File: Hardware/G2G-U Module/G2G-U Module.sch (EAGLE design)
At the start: 4 parts, among them J1 GROVE-4P-2.0-SMD-FEMALE-REINF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

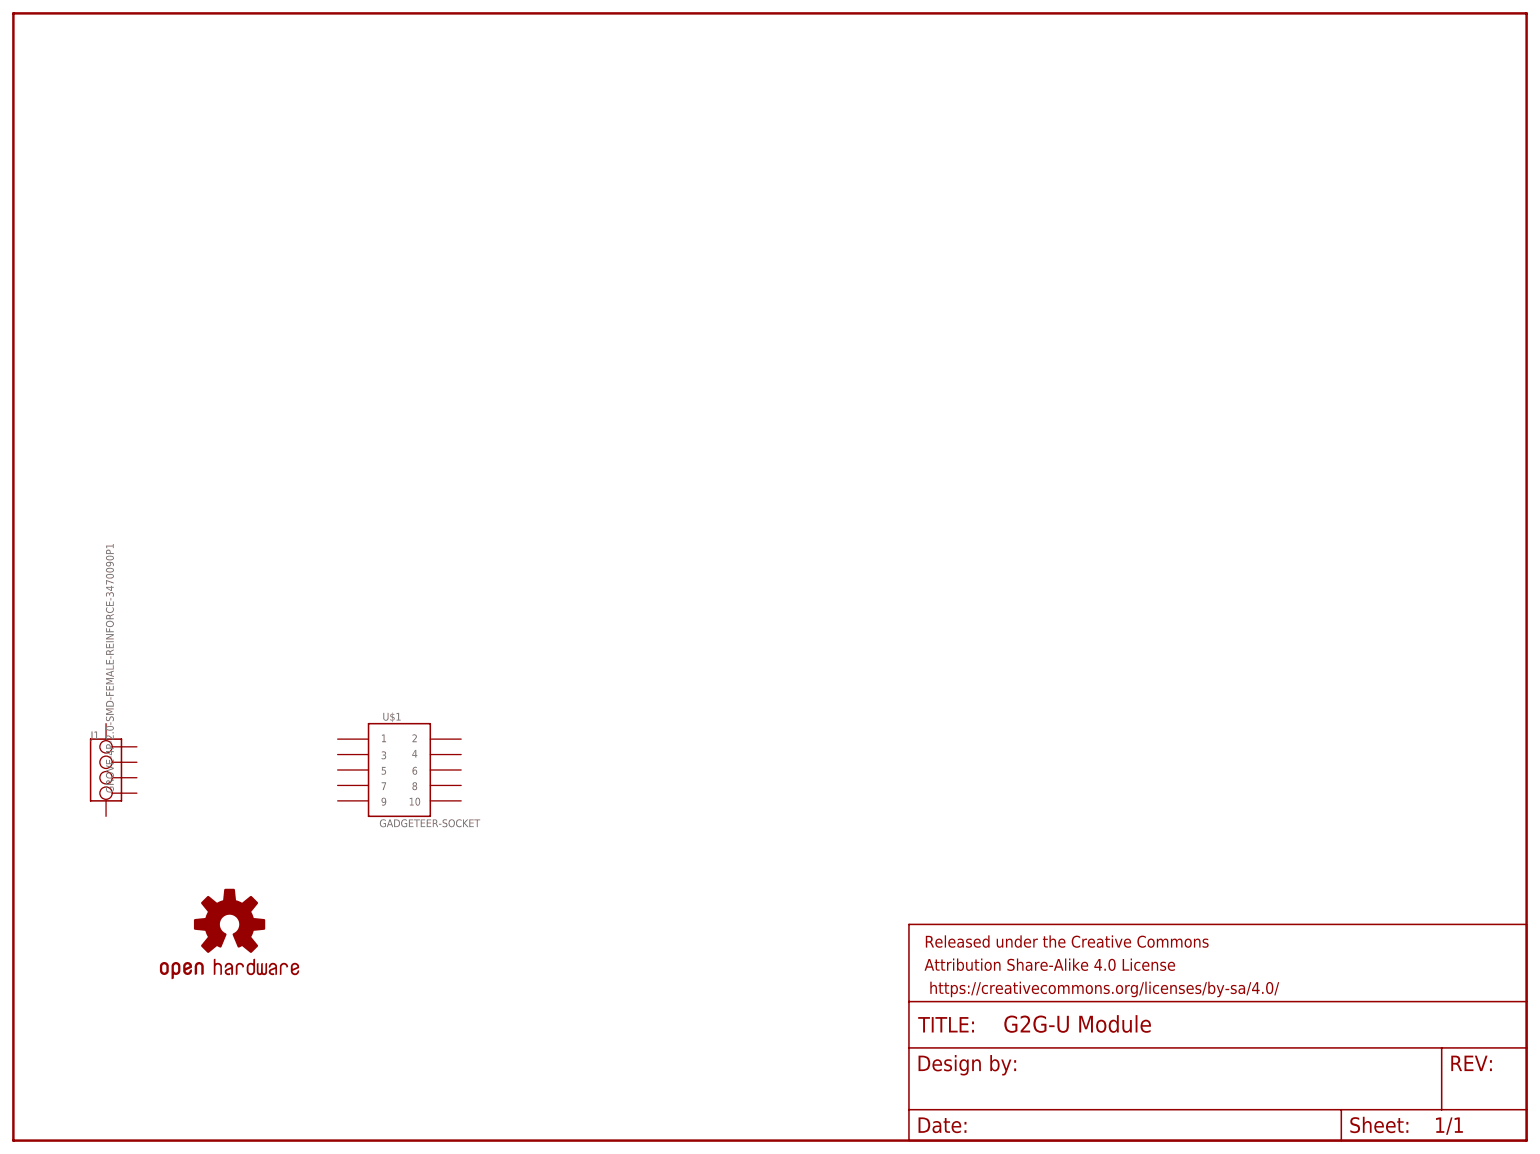
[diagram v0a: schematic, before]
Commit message: Added initial schematic of GSG-U module (using Gadgeteer socket instead of plug...).
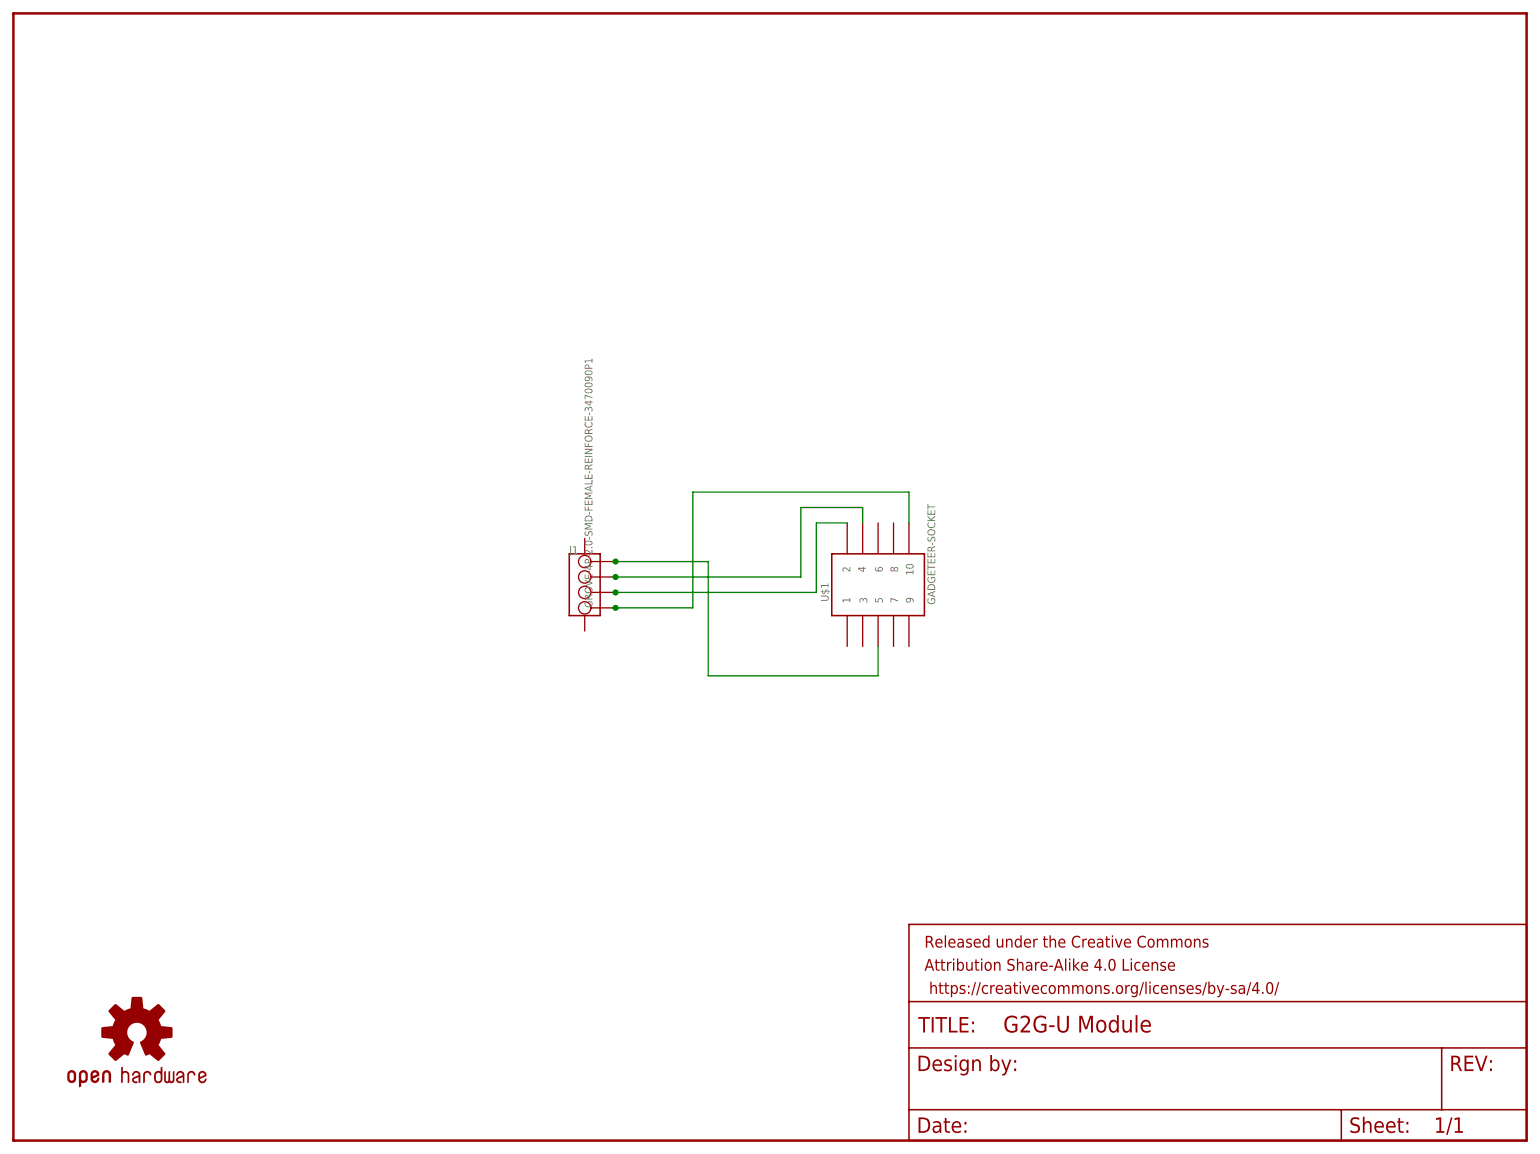
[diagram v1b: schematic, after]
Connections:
- new net N$1: J1.1, U$1.P$5
- new net N$2: J1.2, U$1.P$4
- new net N$3: J1.3, U$1.P$2
- new net N$4: J1.4, U$1.P$10
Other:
- moved on the sheet: J1, U$1
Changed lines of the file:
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@@
 </plain>
 <instances>
-<instance part="J1" gate="J" x="15.24" y="60.96"/>
-<instance part="U$1" gate="G$1" x="63.5" y="60.96"/>
-<instance part="LOGO1" gate="G$1" x="35.56" y="35.56"/>
+<instance part="J1" gate="J" x="93.98" y="91.44"/>
+<instance part="U$1" gate="G$1" x="142.24" y="91.44" rot="R90"/>
+<instance part="LOGO1" gate="G$1" x="20.32" y="17.78"/>
 <instance part="FRAME1" gate="G$1" x="0" y="0"/>
 <instance part="FRAME1" gate="G$2" x="147.32" y="0"/>
@@
 </busses>
 <nets>
+<net name="N$1" class="0">
+<segment>
+<wire x1="98.552" y1="95.25" x2="99.06" y2="95.25" width="0.1524" layer="91"/>
+<wire x1="99.06" y1="95.25" x2="114.3" y2="95.25" width="0.1524" layer="91"/>
+<wire x1="114.3" y1="95.25" x2="114.3" y2="76.454" width="0.1524" layer="91"/>
+<pinref part="U$1" gate="G$1" pin="P$5"/>
+<wire x1="114.3" y1="76.454" x2="142.24" y2="76.454" width="0.1524" layer="91"/>
+<wire x1="142.24" y1="76.454" x2="142.24" y2="81.28" width="0.1524" layer="91"/>
+<pinref part="J1" gate="J" pin="1"/>
+<junction x="99.06" y="95.25"/>
+</segment>
+</net>
+<net name="N$2" class="0">
+<segment>
+<wire x1="98.552" y1="92.71" x2="99.06" y2="92.71" width="0.1524" layer="91"/>
+<wire x1="99.06" y1="92.71" x2="129.54" y2="92.71" width="0.1524" layer="91"/>
+<wire x1="129.54" y1="92.71" x2="129.54" y2="104.14" width="0.1524" layer="91"/>
+<pinref part="U$1" gate="G$1" pin="P$4"/>
+<wire x1="129.54" y1="104.14" x2="139.7" y2="104.14" width="0.1524" layer="91"/>
+<wire x1="139.7" y1="104.14" x2="139.7" y2="101.6" width="0.1524" layer="91"/>
+<pinref part="J1" gate="J" pin="2"/>
+<junction x="99.06" y="92.71"/>
+</segment>
+</net>
+<net name="N$3" class="0">
+<segment>
+<wire x1="98.552" y1="90.17" x2="99.06" y2="90.17" width="0.1524" layer="91"/>
+<wire x1="99.06" y1="90.17" x2="132.08" y2="90.17" width="0.1524" layer="91"/>
+<wire x1="132.08" y1="90.17" x2="132.08" y2="101.6" width="0.1524" layer="91"/>
+<pinref part="U$1" gate="G$1" pin="P$2"/>
+<wire x1="132.08" y1="101.6" x2="137.16" y2="101.6" width="0.1524" layer="91"/>
+<pinref part="J1" gate="J" pin="3"/>
+<junction x="99.06" y="90.17"/>
+</segment>
+</net>
+<net name="N$4" class="0">
+<segment>
+<wire x1="98.552" y1="87.63" x2="99.06" y2="87.63" width="0.1524" layer="91"/>
+<wire x1="99.06" y1="87.63" x2="111.76" y2="87.63" width="0.1524" layer="91"/>
+<wire x1="111.76" y1="87.63" x2="111.76" y2="106.68" width="0.1524" layer="91"/>
+<pinref part="U$1" gate="G$1" pin="P$10"/>
+<wire x1="111.76" y1="106.68" x2="147.32" y2="106.68" width="0.1524" layer="91"/>
+<wire x1="147.32" y1="106.68" x2="147.32" y2="101.6" width="0.1524" layer="91"/>
+<pinref part="J1" gate="J" pin="4"/>
+<junction x="99.06" y="87.63"/>
+</segment>
+</net>
 </nets>
 </sheet>

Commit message: First draft of G2G-U before ground plane.
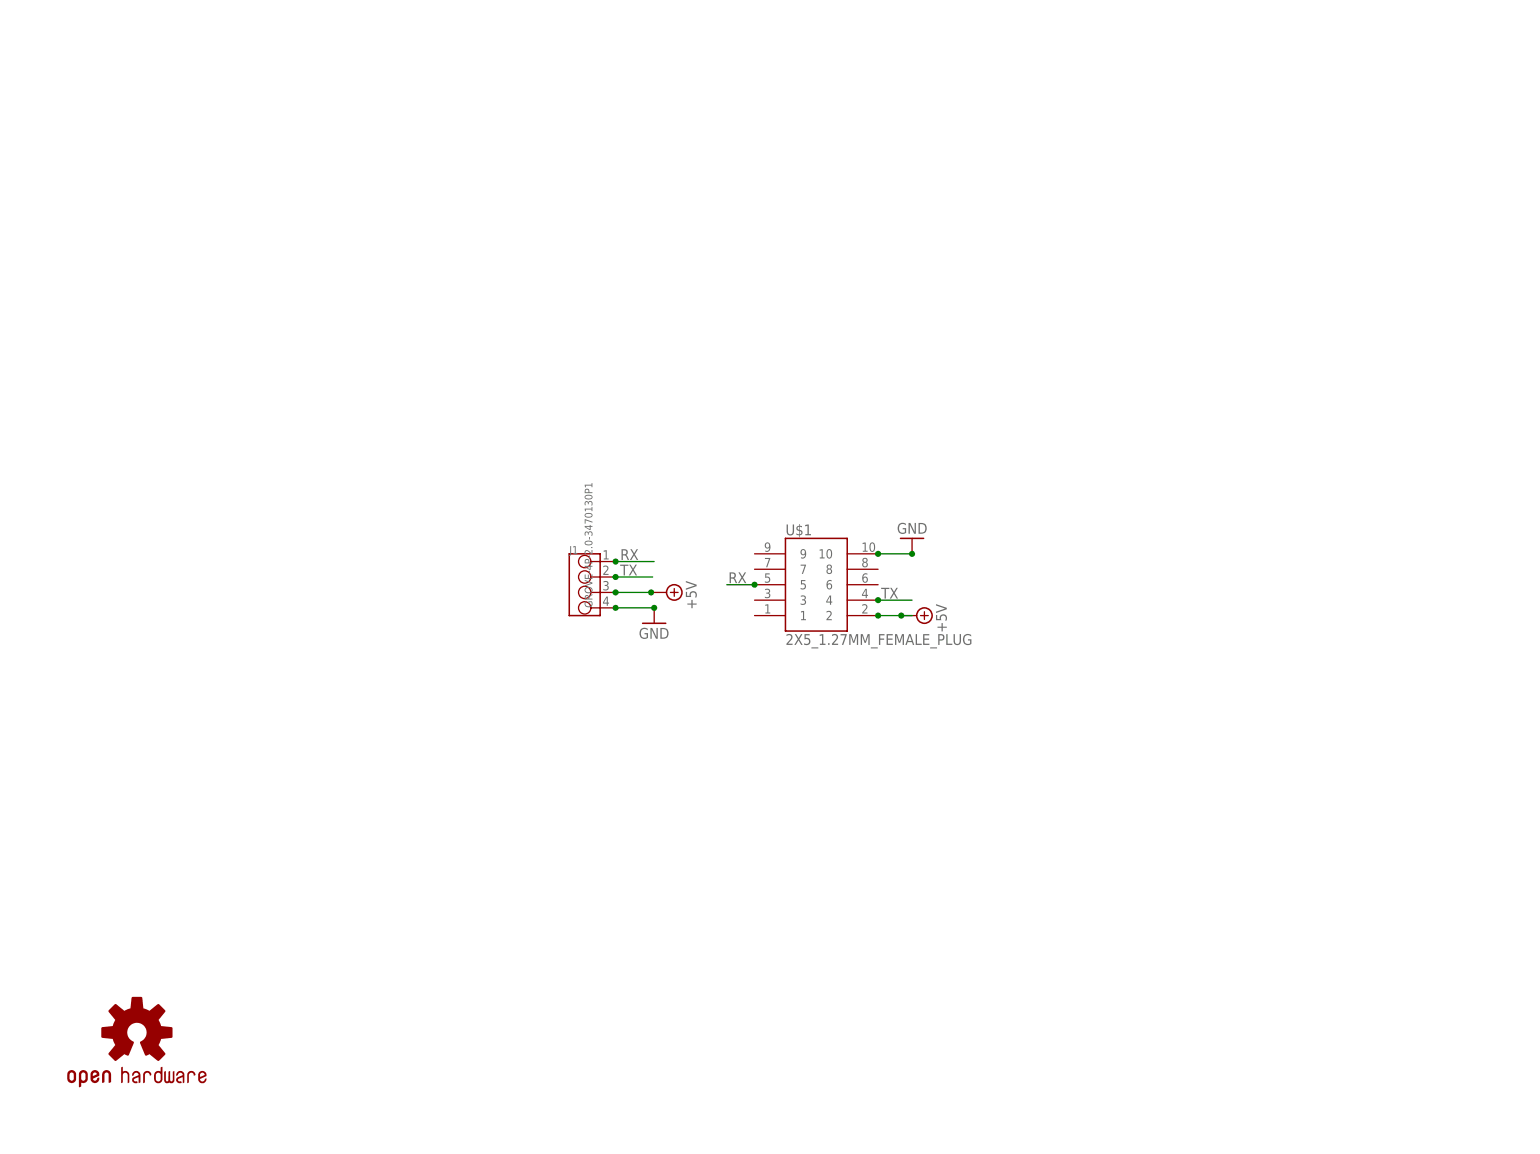
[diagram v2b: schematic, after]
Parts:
- removed FRAME1: FRAME-LETTER, SparkFun-Aesthetics:FRAME-LETTER
- J1: value GROVE-4P-2.0-SMD-FEMALE-REINFORCE-3470090P1 -> GROVE-4P-2.0-3470130P1; device Connector:GROVE-4P-2.0-SMD-FEMALE-REINFORCE-3470090P1 -> SoftDust:GROVE-4P-2.0-3470130P1
- U$1: value GADGETEER-SOCKET -> 2X5_1.27MM_FEMALE_PLUG; device SoftDust:GADGETEER-SOCKET -> SoftDust:2X5_1.27MM_FEMALE_PLUG
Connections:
- removed net N$1: J1.1, U$1.P$5
- removed net N$2: J1.2, U$1.P$4
- removed net N$3: J1.3, U$1.P$2
- removed net N$4: J1.4, U$1.P$10
- new net +5V: J1.3, U$1.2
- new net GND: J1.4, U$1.10
- new net RX: J1.1, U$1.5
- new net TX: J1.2, U$1.4
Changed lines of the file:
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@@
 <layer number="251" name="SMDround" color="12" fill="11" visible="no" active="no"/>
 <layer number="254" name="OrgLBR" color="13" fill="1" visible="no" active="no"/>
+<layer number="255" name="INPROGRESS" color="7" fill="1" visible="yes" active="yes"/>
 </layers>
 <schematic xreflabel="%F%N/%S.%C%R" xrefpart="/%S.%C%R">
@@
 </classes>
 <parts>
-<part name="J1" library="Connector" deviceset="GROVE-4P-2.0-SMD-FEMALE-REINFORCE" device="-3470090P1"/>
-<part name="U$1" library="SoftDust" deviceset="GADGETEER-SOCKET" device=""/>
+<part name="J1" library="SoftDust" deviceset="GROVE-4P-2.0" device="-3470130P1"/>
+<part name="U$1" library="SoftDust" deviceset="2X5_1.27MM_FEMALE_PLUG" device=""/>
 <part name="LOGO1" library="SparkFun-Aesthetics" deviceset="OSHW-LOGO" device="S"/>
-<part name="FRAME1" library="SparkFun-Aesthetics" deviceset="FRAME-LETTER" device=""/>
+<part name="GND1" library="supply1" deviceset="GND" device=""/>
+<part name="GND2" library="supply1" deviceset="GND" device=""/>
+<part name="SUPPLY1" library="supply2" deviceset="+5V" device=""/>
+<part name="SUPPLY2" library="supply2" deviceset="+5V" device=""/>
 </parts>
 <sheets>
@@
 <instances>
 <instance part="J1" gate="J" x="93.98" y="91.44"/>
-<instance part="U$1" gate="G$1" x="142.24" y="91.44" rot="R90"/>
+<instance part="U$1" gate="G$1" x="132.08" y="91.44"/>
 <instance part="LOGO1" gate="G$1" x="20.32" y="17.78"/>
-<instance part="FRAME1" gate="G$1" x="0" y="0"/>
-<instance part="FRAME1" gate="G$2" x="147.32" y="0"/>
+<instance part="GND1" gate="1" x="105.41" y="85.09"/>
+<instance part="GND2" gate="1" x="147.828" y="99.06" rot="R180"/>
+<instance part="SUPPLY1" gate="+5V" x="107.442" y="90.17" rot="R270"/>
+<instance part="SUPPLY2" gate="+5V" x="148.59" y="86.36" rot="R270"/>
 </instances>
 <busses>
 </busses>
 <nets>
-<net name="N$1" class="0">
+<net name="TX" class="0">
 <segment>
-<wire x1="98.552" y1="95.25" x2="99.06" y2="95.25" width="0.1524" layer="91"/>
-<wire x1="99.06" y1="95.25" x2="114.3" y2="95.25" width="0.1524" layer="91"/>
-<wire x1="114.3" y1="95.25" x2="114.3" y2="76.454" width="0.1524" layer="91"/>
-<pinref part="U$1" gate="G$1" pin="P$5"/>
-<wire x1="114.3" y1="76.454" x2="142.24" y2="76.454" width="0.1524" layer="91"/>
-<wire x1="142.24" y1="76.454" x2="142.24" y2="81.28" width="0.1524" layer="91"/>
-<pinref part="J1" gate="J" pin="1"/>
-<junction x="99.06" y="95.25"/>
+<pinref part="U$1" gate="G$1" pin="4"/>
+<wire x1="142.24" y1="88.9" x2="147.828" y2="88.9" width="0.1524" layer="91"/>
+<junction x="142.24" y="88.9"/>
+<label x="142.748" y="89.154" size="1.778" layer="95"/>
+</segment>
+<segment>
+<pinref part="J1" gate="J" pin="2"/>
+<wire x1="98.552" y1="92.71" x2="99.06" y2="92.71" width="0.1524" layer="91"/>
+<wire x1="99.06" y1="92.71" x2="105.156" y2="92.71" width="0.1524" layer="91"/>
+<junction x="99.06" y="92.71"/>
+<label x="99.822" y="92.964" size="1.778" layer="95"/>
 </segment>
 </net>
-<net name="N$2" class="0">
+<net name="GND" class="0">
 <segment>
-<wire x1="98.552" y1="92.71" x2="99.06" y2="92.71" width="0.1524" layer="91"/>
-<wire x1="99.06" y1="92.71" x2="129.54" y2="92.71" width="0.1524" layer="91"/>
-<wire x1="129.54" y1="92.71" x2="129.54" y2="104.14" width="0.1524" layer="91"/>
-<pinref part="U$1" gate="G$1" pin="P$4"/>
-<wire x1="129.54" y1="104.14" x2="139.7" y2="104.14" width="0.1524" layer="91"/>
-<wire x1="139.7" y1="104.14" x2="139.7" y2="101.6" width="0.1524" layer="91"/>
-<pinref part="J1" gate="J" pin="2"/>
-<junction x="99.06" y="92.71"/>
+<wire x1="141.986" y1="96.52" x2="142.24" y2="96.52" width="0.1524" layer="91"/>
+<pinref part="U$1" gate="G$1" pin="10"/>
+<junction x="142.24" y="96.52"/>
+<wire x1="142.24" y1="96.52" x2="147.828" y2="96.52" width="0.1524" layer="91"/>
+<pinref part="GND2" gate="1" pin="GND"/>
+<junction x="147.828" y="96.52"/>
+</segment>
+<segment>
+<wire x1="98.806" y1="87.63" x2="99.06" y2="87.63" width="0.1524" layer="91"/>
+<pinref part="J1" gate="J" pin="4"/>
+<junction x="99.06" y="87.63"/>
+<wire x1="99.06" y1="87.63" x2="105.41" y2="87.63" width="0.1524" layer="91"/>
+<pinref part="GND1" gate="1" pin="GND"/>
+<junction x="105.41" y="87.63"/>
 </segment>
 </net>
-<net name="N$3" class="0">
+<net name="RX" class="0">
 <segment>
-<wire x1="98.552" y1="90.17" x2="99.06" y2="90.17" width="0.1524" layer="91"/>
-<wire x1="99.06" y1="90.17" x2="132.08" y2="90.17" width="0.1524" layer="91"/>
-<wire x1="132.08" y1="90.17" x2="132.08" y2="101.6" width="0.1524" layer="91"/>
-<pinref part="U$1" gate="G$1" pin="P$2"/>
-<wire x1="132.08" y1="101.6" x2="137.16" y2="101.6" width="0.1524" layer="91"/>
+<wire x1="122.174" y1="91.44" x2="121.92" y2="91.44" width="0.1524" layer="91"/>
+<pinref part="U$1" gate="G$1" pin="5"/>
+<junction x="121.92" y="91.44"/>
+<wire x1="121.92" y1="91.44" x2="117.348" y2="91.44" width="0.1524" layer="91"/>
+<label x="117.602" y="91.694" size="1.778" layer="95"/>
+</segment>
+<segment>
+<pinref part="J1" gate="J" pin="1"/>
+<wire x1="99.06" y1="95.25" x2="105.41" y2="95.25" width="0.1524" layer="91"/>
+<junction x="99.06" y="95.25"/>
+<label x="99.822" y="95.504" size="1.778" layer="95"/>
+</segment>
+</net>
+<net name="+5V" class="0">
+<segment>
+<wire x1="99.06" y1="90.17" x2="104.902" y2="90.17" width="0.1524" layer="91"/>
 <pinref part="J1" gate="J" pin="3"/>
 <junction x="99.06" y="90.17"/>
+<wire x1="104.902" y1="90.17" x2="105.156" y2="90.17" width="0.1524" layer="91"/>
+<wire x1="98.552" y1="90.17" x2="99.06" y2="90.17" width="0.1524" layer="91"/>
+<pinref part="SUPPLY1" gate="+5V" pin="+5V"/>
+<junction x="104.902" y="90.17"/>
+</segment>
+<segment>
+<pinref part="U$1" gate="G$1" pin="2"/>
+<wire x1="147.828" y1="86.36" x2="146.05" y2="86.36" width="0.1524" layer="91"/>
+<junction x="142.24" y="86.36"/>
+<pinref part="SUPPLY2" gate="+5V" pin="+5V"/>
+<wire x1="146.05" y1="86.36" x2="142.24" y2="86.36" width="0.1524" layer="91"/>
+<junction x="146.05" y="86.36"/>
 </segment>
 </net>
-<net name="N$4" class="0">
-<segment>
-<wire x1="98.552" y1="87.63" x2="99.06" y2="87.63" width="0.1524" layer="91"/>
-<wire x1="99.06" y1="87.63" x2="111.76" y2="87.63" width="0.1524" layer="91"/>
-<wire x1="111.76" y1="87.63" x2="111.76" y2="106.68" width="0.1524" layer="91"/>
-<pinref part="U$1" gate="G$1" pin="P$10"/>
-<wire x1="111.76" y1="106.68" x2="147.32" y2="106.68" width="0.1524" layer="91"/>
-<wire x1="147.32" y1="106.68" x2="147.32" y2="101.6" width="0.1524" layer="91"/>
-<pinref part="J1" gate="J" pin="4"/>
-<junction x="99.06" y="87.63"/>
-</segment>
-</net>
